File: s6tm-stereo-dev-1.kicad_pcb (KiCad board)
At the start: 4 copper layers, 85 x 80 mm, 190 parts, among them J1 Micro_SD_Card_Det1, J2 Conn_01x04_Pin, J3 USB_C_Receptacle_USB2.0_14P, J4 Conn_01x02, J5 AudioJack4, J6 Conn_01x02, J7 Conn_01x02, J8 Conn_01x02, Q1 Q_NMOS, Q2 Q_NMOS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

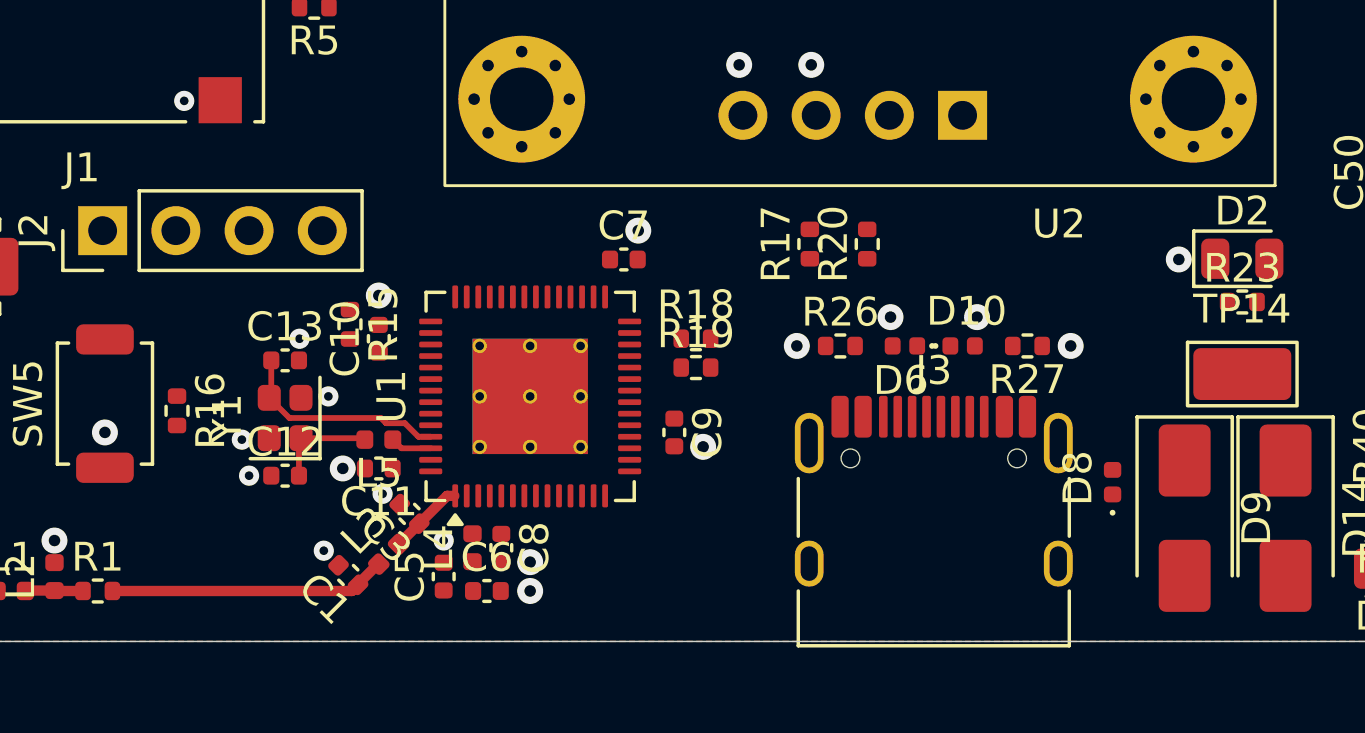
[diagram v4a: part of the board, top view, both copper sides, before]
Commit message: pcb: add uart routing
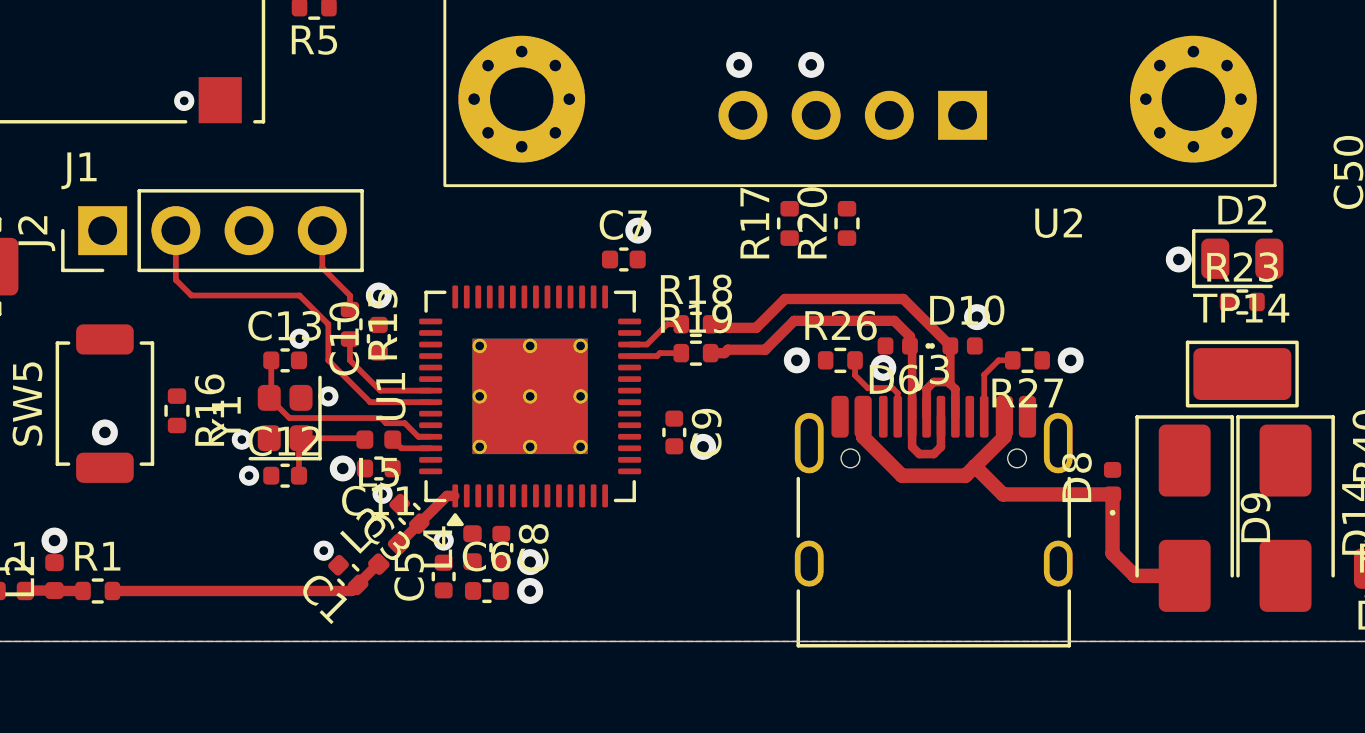
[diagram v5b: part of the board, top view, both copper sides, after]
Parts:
- moved R17 1.00 mm to (150.8, 132.5)
- moved R20 1.00 mm to (152.7, 132.5)
- moved R18 0.50 mm to (147.5, 136.0)
- moved R19 0.50 mm to (147.5, 137.0)
- moved R26 0.50 mm to (152.5, 137.2)
- moved R27 0.50 mm to (159.0, 137.2)
- moved D6 0.25 mm to (154.5, 136.8)
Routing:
- net +Vbus: track 0.00 -> 17.5 mm
- net /D+: track 0.00 -> 13.9 mm
- net /D-: track 0.00 -> 13.7 mm
- net /U0RXD: track 0.00 -> 13.0 mm
- net /U0TXD: track 0.00 -> 3.97 mm
- net Net-(J2-Pin_4): track 0.00 -> 3.14 mm
- net Net-(J3-CC1): track 0.00 -> 3.07 mm
- net Net-(J3-CC2): track 0.00 -> 2.65 mm
- net /ESP_D+: track 0.00 -> 2.08 mm
- net /ESP_D-: track 0.00 -> 1.83 mm

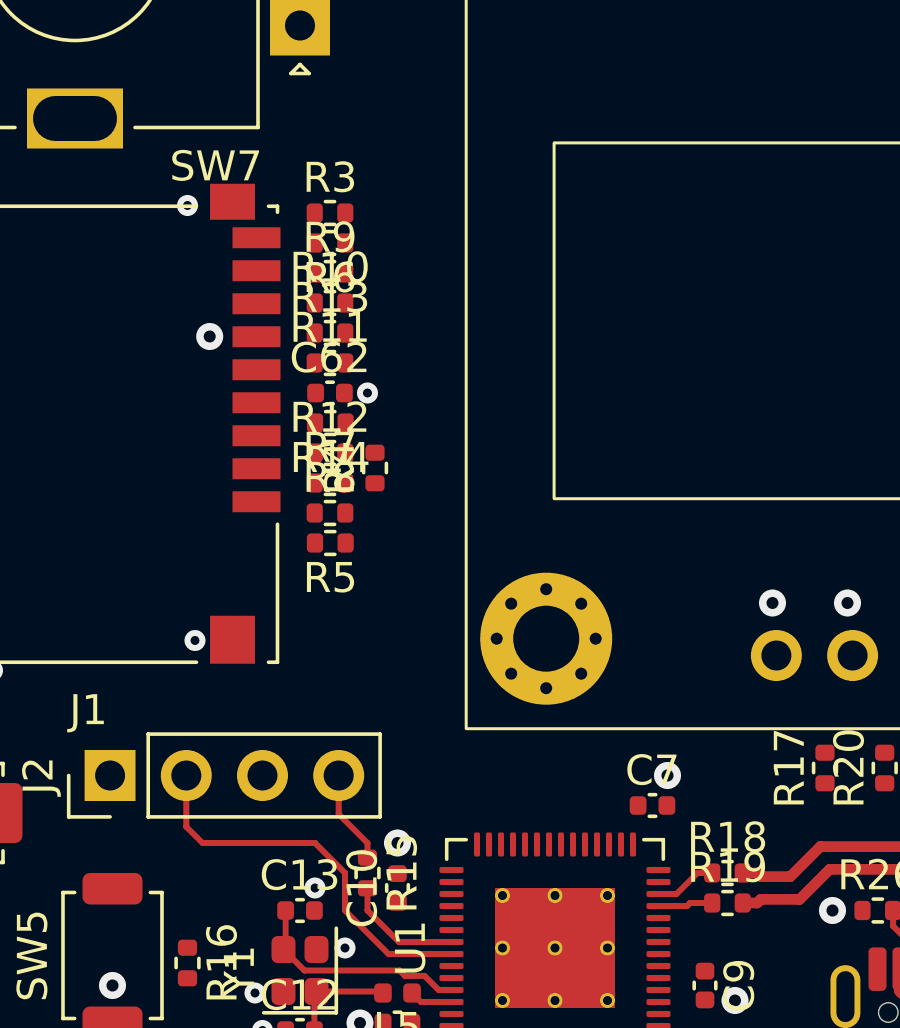
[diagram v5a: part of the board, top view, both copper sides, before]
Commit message: pcb: add sd card routing
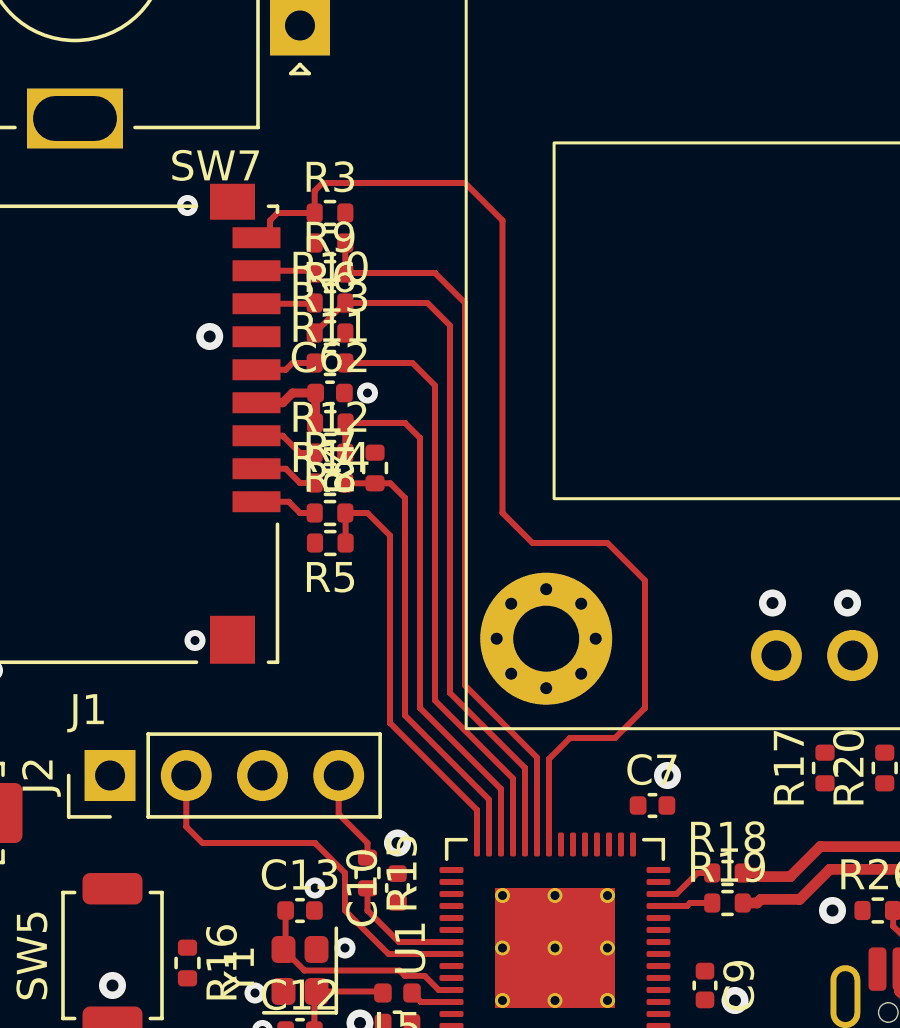
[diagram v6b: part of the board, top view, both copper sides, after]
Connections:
- R10 pad 2: Net-(U1-GPIO34) -> Net-(U1-GPIO33)
- R11 pad 2: Net-(U1-GPIO33) -> Net-(U1-GPIO34)
- R12 pad 2: Net-(U1-SPICLK_P/GPIO47) -> Net-(U1-GPIO35)
- R13 pad 1: Net-(U1-GPIO34) -> Net-(U1-GPIO33)
- R14 pad 1: Net-(U1-SPICLK_P/GPIO47) -> Net-(U1-GPIO35)
- R4 pad 1: Net-(U1-GPIO37) -> Net-(U1-GPIO36)
- R5 pad 1: Net-(U1-GPIO36) -> Net-(U1-GPIO37)
- R6 pad 1: Net-(U1-GPIO35) -> Net-(U1-SPICLK_P/GPIO47)
- R7 pad 2: Net-(U1-GPIO37) -> Net-(U1-GPIO36)
- R8 pad 2: Net-(U1-GPIO36) -> Net-(U1-GPIO37)
- R9 pad 2: Net-(U1-GPIO35) -> Net-(U1-SPICLK_P/GPIO47)
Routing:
- net Net-(J1-DET): track 0.00 -> 36.6 mm
- net Net-(U1-SPICLK_P/GPIO47): track 0.00 -> 24.4 mm
- net Net-(U1-GPIO33): track 0.00 -> 23.6 mm
- net Net-(U1-GPIO34): track 0.00 -> 19.7 mm
- net Net-(U1-GPIO35): track 0.00 -> 18.4 mm
- net Net-(U1-GPIO36): track 0.00 -> 14.9 mm
- net Net-(U1-GPIO37): track 0.00 -> 14.3 mm
- net +3V3: track 0.00 -> 3.11 mm
- net Net-(J1-CMD): track 0.00 -> 2.18 mm
- net Net-(J1-DAT3/CD): track 0.00 -> 2.14 mm
- net Net-(J1-DAT2): track 0.00 -> 2.10 mm
- net Net-(J1-CLK): track 0.00 -> 2.03 mm
- net Net-(J1-DAT1): track 0.00 -> 1.97 mm
- net Net-(J1-DAT0): track 0.00 -> 1.95 mm
